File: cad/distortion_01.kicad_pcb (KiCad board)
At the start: 2 copper layers, 147.5 x 81.2 mm, 103 parts, among them CON101 Ext_PSU, J101 JACK_IN, J102 JACK_OUT, P101 Battery_conn, P102 BYPASS_SWITCH, P103 CONN_01X03, P104 CONN_01X03, P105 CONN_01X03, P106 CONN_01X03, Q101 BS170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

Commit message: Finished layout.
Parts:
- moved C104 3.25 mm to (86.8, 79.8)
- moved R109 2.61 mm to (45.0, 81.2), turned to 0 degrees
- moved C125 1.75 mm to (66.5, 77.8)
- moved R122 1.50 mm to (64.0, 77.8)
- moved R113 1.00 mm to (43.8, 72.8)
- moved R121 0.79 mm to (72.0, 75.8)
- moved R120 0.56 mm to (70.2, 79.2)
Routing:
- net +9V: track 219.3 -> 339.7 mm, vias 7 -> 10
- net VCOM: track 116.5 -> 201.0 mm, vias 4 -> 6
- net Net-(C105-Pad2): track 31.1 -> 64.6 mm, vias 1 -> 3
- net GND: track 162.3 -> 184.1 mm, vias 15 -> 16
- net Net-(C108-Pad1): track 7.12 -> 21.0 mm
- net Net-(R123-Pad1): track 35.9 -> 49.6 mm
- net Net-(C115-Pad2): track 55.3 -> 64.4 mm, vias 2 -> 4
- net Net-(D106-Pad1): track 62.7 -> 68.7 mm
- net /audio_fx_in: track 74.6 -> 69.4 mm
- net Net-(P105-Pad3): track 47.5 -> 52.2 mm
- net Net-(C111-Pad1): track 17.9 -> 13.9 mm
- net Net-(C106-Pad1): track 2.66 -> 6.61 mm
- net Net-(C125-Pad1): track 10.8 -> 14.4 mm
- net /bypass_cmd: track 111.9 -> 114.9 mm
- net /~bypass_cmd~: track 72.7 -> 75.6 mm
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- added copper zone on B.Cu, net GNDPWR

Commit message: Corrected layout.
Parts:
- moved R123 1.80 mm to (69.8, 51.2), turned to 270 degrees
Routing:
- net VCOM: track 201.0 -> 242.8 mm, vias 6 -> 7
- net Net-(C114-Pad1): track 28.0 -> 37.8 mm
- net /audio_prunes_out: track 56.0 -> 62.8 mm
- net Net-(C115-Pad2): track 64.4 -> 65.6 mm
- net Net-(C105-Pad2): track 64.6 -> 65.7 mm
- net Net-(D111-Pad1): track 31.3 -> 32.2 mm
- net Net-(R123-Pad1): track 49.6 -> 50.3 mm
- net Net-(C112-Pad2): track 14.9 -> 14.3 mm
- net Net-(C109-Pad2): track 31.9 -> 32.5 mm
- net +9V: track 339.7 -> 340.3 mm

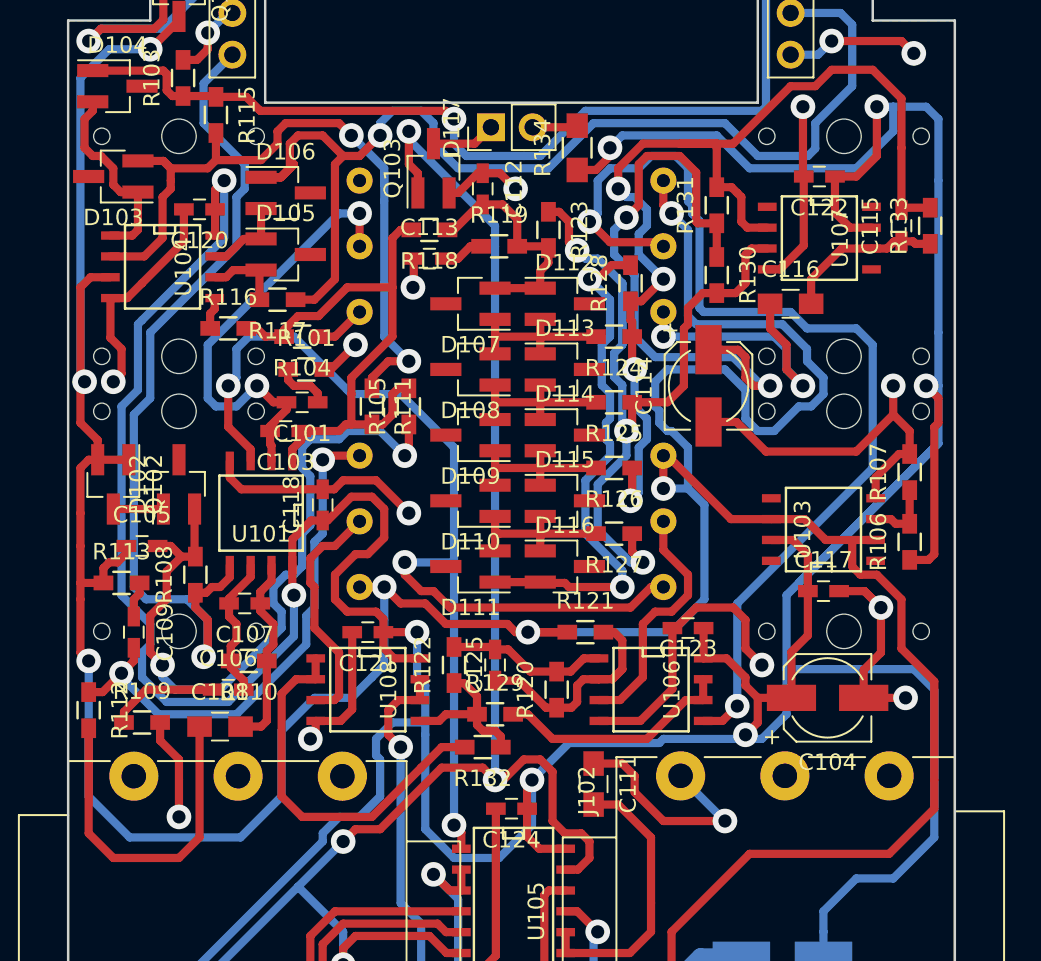
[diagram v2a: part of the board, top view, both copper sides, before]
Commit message: Corrected pots pinout and layout.
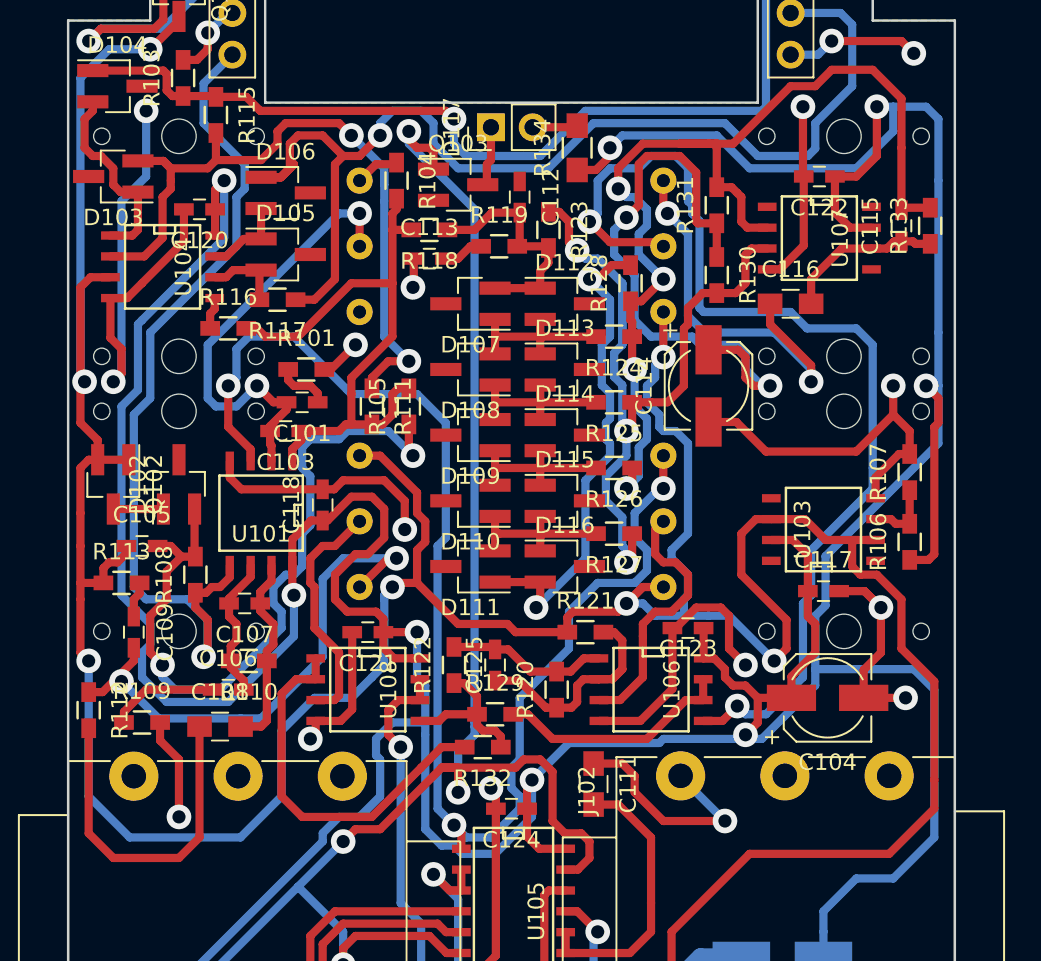
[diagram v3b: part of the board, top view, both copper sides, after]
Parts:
- moved R104 11.1 mm to (60.5, 48.2), turned to 270 degrees
- moved C112 2.30 mm to (68.0, 49.2)
- moved Q103 1.80 mm to (64.2, 48.5), turned to 0 degrees
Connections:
- RV_DRY101 pad 1: /audio_fx_in -> VCOM
- RV_DRY101 pad 3: VCOM -> /audio_fx_in
- RV_GAIN101 pad 1: (no net) -> Net-(R104-Pad1)
- RV_GAIN101 pad 3: Net-(R104-Pad1) -> (no net)
- RV_OCD101 pad 1: Net-(C109-Pad2) -> VCOM
- RV_OCD101 pad 3: VCOM -> Net-(C109-Pad2)
- RV_PRUNES101 pad 1: Net-(C116-Pad1) -> VCOM
- RV_PRUNES101 pad 3: VCOM -> Net-(C116-Pad1)
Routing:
- net VCOM: track 242.8 -> 228.1 mm
- net GND: track 184.1 -> 198.4 mm, vias 16 -> 17
- net +9V: track 340.3 -> 326.4 mm
- net /audio_fx_in: track 69.4 -> 82.5 mm
- net Net-(C116-Pad1): track 17.8 -> 24.3 mm
- net /bypass_cmd: track 114.9 -> 117.3 mm
- net /audio_gain: track 35.0 -> 36.9 mm
- net Net-(D111-Pad1): track 32.2 -> 30.3 mm
- net /audio_prunes_out: track 62.8 -> 64.5 mm
- net Net-(R123-Pad1): track 50.3 -> 48.9 mm
- net Net-(C115-Pad2): track 65.6 -> 64.3 mm
- net Net-(RV_DRY101-Pad2): track 15.1 -> 15.9 mm
- net Net-(C105-Pad2): track 65.7 -> 66.2 mm

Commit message: Continued layout
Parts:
- RV_DRY101, RV_GAIN101, RV_OCD101, RV_PRUNES101: footprint flax_lib:alpha_rv141F -> flax_lib:PTV09; moved to F.Cu
- moved RV_GAIN101 10.3 mm to (57.5, 51.0), turned to 90 degrees
- moved RV_PRUNES101 10.3 mm to (77.5, 51.0), turned to 270 degrees
- moved RV_DRY101 10.3 mm to (77.5, 68.2), turned to 270 degrees
- moved RV_OCD101 10.3 mm to (57.5, 68.2), turned to 90 degrees
- moved R115 5.40 mm to (54.8, 45.5), turned to 180 degrees
- moved C117 5.27 mm to (81.2, 72.8), turned to 180 degrees
- moved C116 4.25 mm to (88.8, 55.8)
- moved C120 3.34 mm to (47.8, 46.8), turned to 90 degrees
- moved U103 3.02 mm to (83.8, 68.2)
- moved U104 2.02 mm to (46.0, 51.5)
- moved C122 1.90 mm to (88.0, 47.2)
- moved R117 1.90 mm to (55.0, 56.2)
- moved D103 1.27 mm to (43.5, 46.8)
- moved R116 1.00 mm to (50.2, 58.2)
- moved U107 0.56 mm to (86.0, 51.2)
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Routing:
- net /audio_prunes_out: track 64.5 -> 0.00 mm, vias 2 -> 0
- net GND: track 198.4 -> 148.1 mm, vias 17 -> 12
- net +9V: track 326.4 -> 290.4 mm, vias 10 -> 9
- net Net-(D103-Pad2): track 44.7 -> 15.4 mm, vias 2 -> 1
- net VCOM: track 228.1 -> 199.0 mm, vias 7 -> 6
- net Net-(D106-Pad1): track 68.7 -> 41.1 mm, vias 1 -> 0
- net Net-(C101-Pad2): track 27.8 -> 4.02 mm, vias 2 -> 0
- net Net-(P105-Pad3): track 52.2 -> 31.1 mm
- net Net-(C109-Pad2): track 32.2 -> 11.4 mm, vias 2 -> 1
- net (no net): track 0.00 -> 19.8 mm, vias 0 -> 2
- net /audio_octave_out: track 54.7 -> 38.4 mm
- net /audio_fx_in: track 82.5 -> 66.8 mm
- net /audio_ocd_out: track 14.5 -> 2.31 mm
- net Net-(D103-Pad1): track 12.1 -> 0.00 mm
- net /audio_gain: track 36.9 -> 26.4 mm
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
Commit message: Finished layout
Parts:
- moved C107 16.4 mm to (43.5, 59.5), turned to 90 degrees
- moved R111 13.8 mm to (60.2, 48.2)
- moved R105 12.3 mm to (50.2, 67.5)
- moved C118 10.1 mm to (47.2, 63.0), turned to 0 degrees
- moved R104 9.78 mm to (61.2, 58.0)
- moved U101 9.75 mm to (48.5, 59.5), turned to 90 degrees
- moved R115 4.60 mm to (50.5, 43.8)
- moved R116 4.42 mm to (47.0, 55.2)
- moved R101 4.04 mm to (58.8, 61.2)
- moved R130 3.02 mm to (81.2, 51.2)
- moved R131 2.61 mm to (80.8, 47.2)
- moved C114 1.95 mm to (81.0, 59.5), turned to 0 degrees
- moved R117 0.71 mm to (54.5, 55.8)
- moved R108 0.56 mm to (48.0, 71.8)
- moved C101 0.50 mm to (54.8, 61.2)
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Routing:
- net /audio_prunes_out: track 0.00 -> 51.6 mm, vias 0 -> 2
- net Net-(C105-Pad2): track 66.2 -> 101.5 mm, vias 3 -> 2
- net +9V: track 290.4 -> 321.4 mm
- net VCOM: track 199.0 -> 228.4 mm
- net Net-(C114-Pad1): track 42.5 -> 16.1 mm, vias 2 -> 0
- net Net-(D106-Pad1): track 41.1 -> 65.9 mm, vias 0 -> 2
- net Net-(C106-Pad2): track 8.92 -> 30.2 mm, vias 0 -> 2
- net Net-(C107-Pad1): track 12.0 -> 31.8 mm, vias 0 -> 2
- net (no net): track 19.8 -> 0.00 mm, vias 2 -> 0
- net Net-(P105-Pad3): track 31.1 -> 49.7 mm, vias 1 -> 2
- net Net-(C101-Pad2): track 4.02 -> 22.6 mm
- net /audio_octave_out: track 38.4 -> 56.4 mm
- net /audio_gain: track 26.4 -> 43.4 mm
- net Net-(C109-Pad2): track 11.4 -> 25.1 mm, vias 1 -> 0
- net Net-(D103-Pad2): track 15.4 -> 28.2 mm, vias 1 -> 0
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
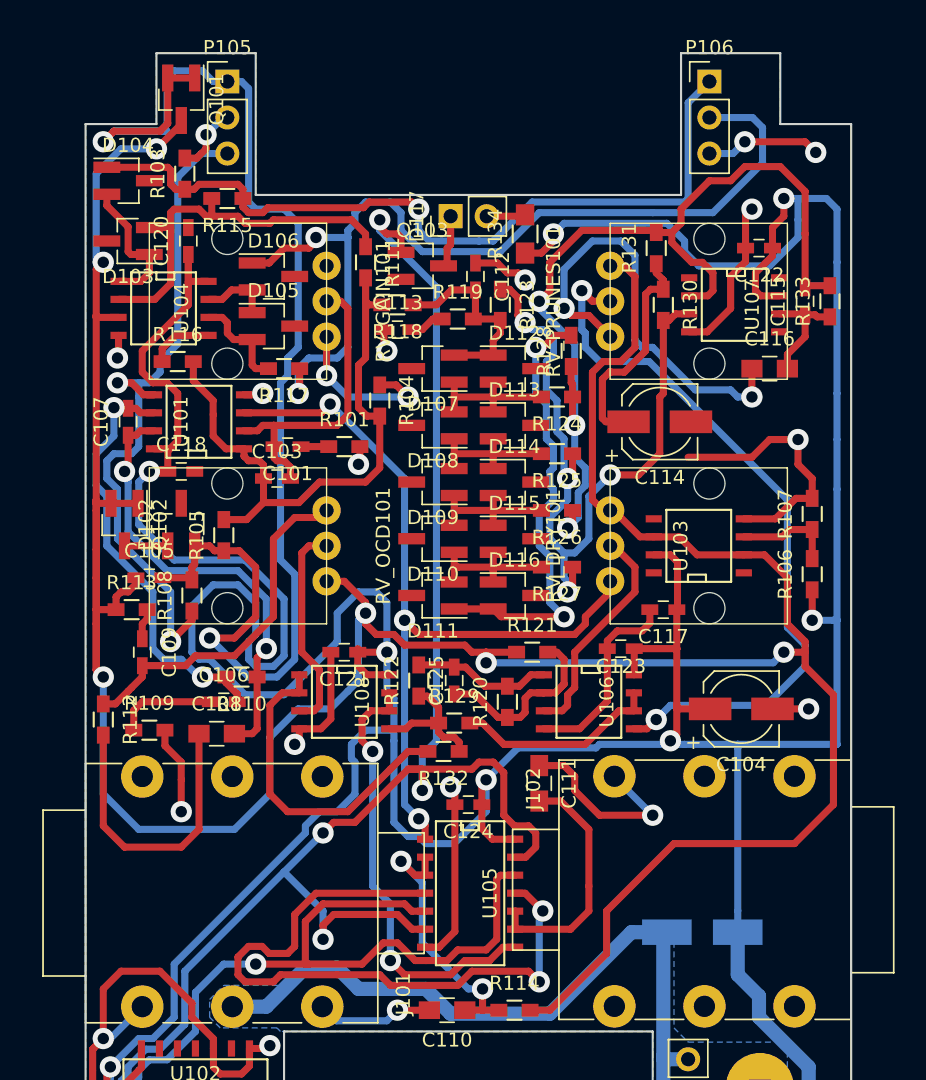
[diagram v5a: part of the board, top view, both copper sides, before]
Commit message: Corrected layout. Added board name.
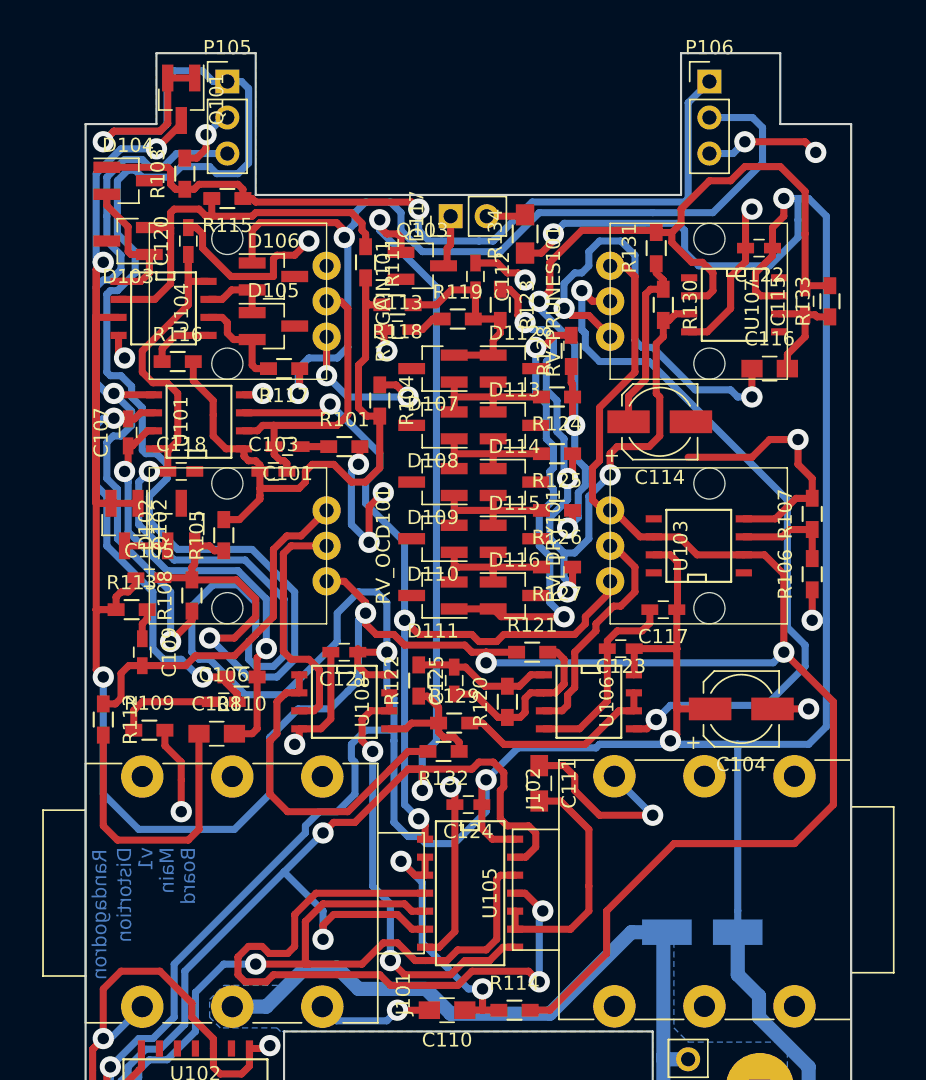
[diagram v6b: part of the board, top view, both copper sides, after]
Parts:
- moved C107 0.75 mm to (43.5, 60.2)
- moved C103 0.56 mm to (53.8, 63.0)
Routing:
- net GND: track 143.6 -> 166.6 mm, vias 15 -> 18
- net VCOM: track 228.4 -> 244.4 mm
- net Net-(C105-Pad2): track 101.5 -> 112.0 mm
- net +9V: track 321.4 -> 328.3 mm
- net Net-(P105-Pad3): track 49.7 -> 54.7 mm
- net Net-(C114-Pad1): track 16.1 -> 12.9 mm
- net /audio_ocd_out: track 14.8 -> 17.4 mm
- net Net-(D106-Pad1): track 65.9 -> 68.0 mm
- net Net-(D103-Pad2): track 28.2 -> 29.6 mm
- net /audio_fx_in: track 57.9 -> 59.1 mm
- net /audio_octave_out: track 56.4 -> 55.4 mm
- net Net-(C109-Pad2): track 25.1 -> 25.9 mm
- net Net-(C101-Pad2): track 22.6 -> 21.8 mm
- net /audio_gain: track 43.4 -> 44.0 mm
- net /bypass_cmd: track 117.3 -> 117.8 mm
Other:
- board text added: "Board"
- board text added: "Distortion"
- board text added: "Main"
- board text added: "v1"

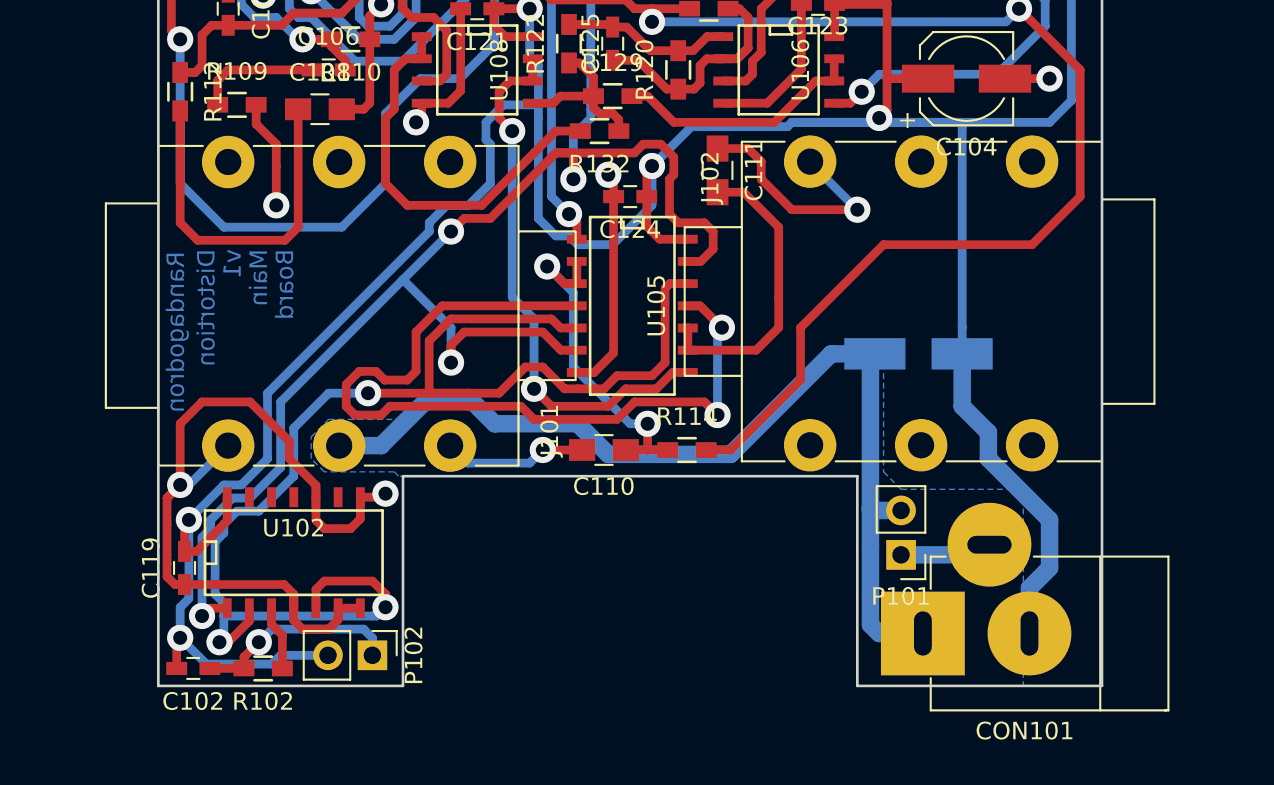
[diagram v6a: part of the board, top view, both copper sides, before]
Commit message: Corrected connectors placement, switch IC and PSU connectors should be swapped for easier routing.
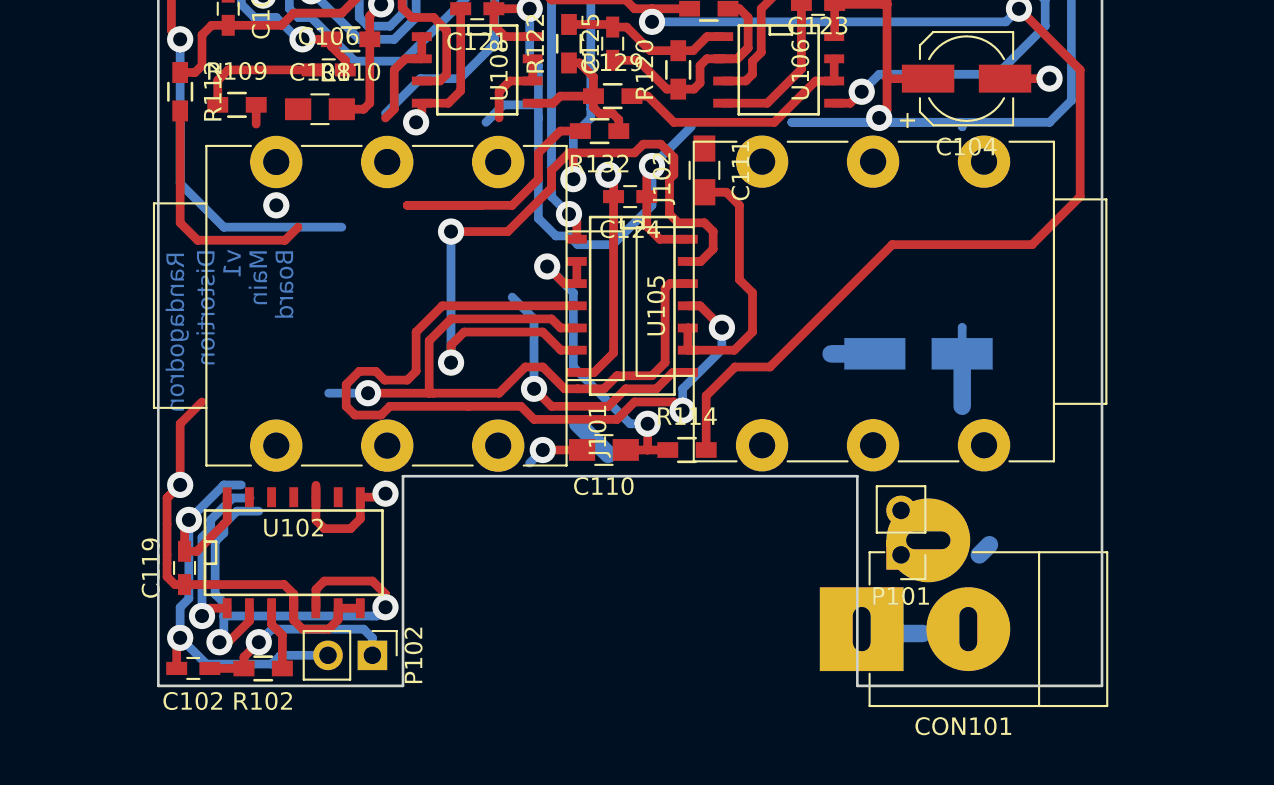
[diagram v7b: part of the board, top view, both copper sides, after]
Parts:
- moved CON101 3.51 mm to (80.8, 111.2)
- moved J101 2.75 mm to (47.2, 100.8)
- moved J102 2.75 mm to (87.8, 84.5)
- moved C111 0.75 mm to (71.8, 85.0)
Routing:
- net GNDPWR: track 57.8 -> 4.35 mm
- net +9V: track 328.3 -> 283.2 mm
- net /bypass_cmd: track 117.8 -> 99.0 mm
- net GND: track 166.6 -> 148.5 mm, vias 18 -> 17
- net +BATT: track 18.5 -> 3.00 mm
- net Net-(C111-Pad1): track 13.9 -> 0.00 mm, vias 1 -> 0
- net /audio_fx_out: track 31.3 -> 20.7 mm, vias 2 -> 1
- net /~bypass_cmd~: track 75.6 -> 67.1 mm
- net VCOM: track 244.4 -> 236.9 mm
- net Net-(C108-Pad1): track 20.6 -> 13.9 mm
- net Net-(CON101-Pad3): track 5.30 -> 0.00 mm
- net Net-(C110-Pad2): track 8.27 -> 3.31 mm
- net (no net): track 0.00 -> 3.55 mm, vias 0 -> 1
- net /audio_jack_out: track 17.1 -> 15.3 mm
- net /audio_bypass: track 48.3 -> 46.8 mm
- removed copper zone on B.Cu, net GNDPWR
